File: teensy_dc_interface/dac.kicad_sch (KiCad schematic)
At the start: 10 parts, among them U1 AK4458VN

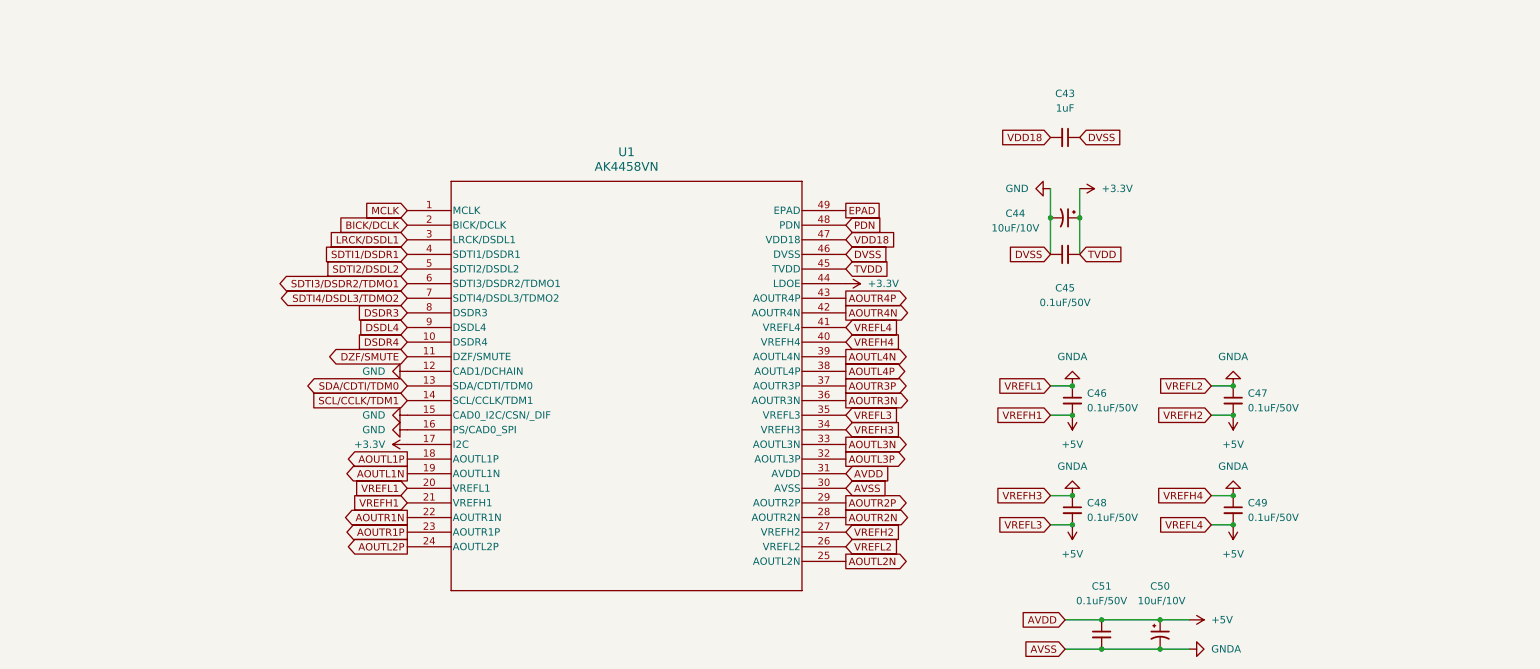
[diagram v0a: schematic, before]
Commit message: teensy to dac connections
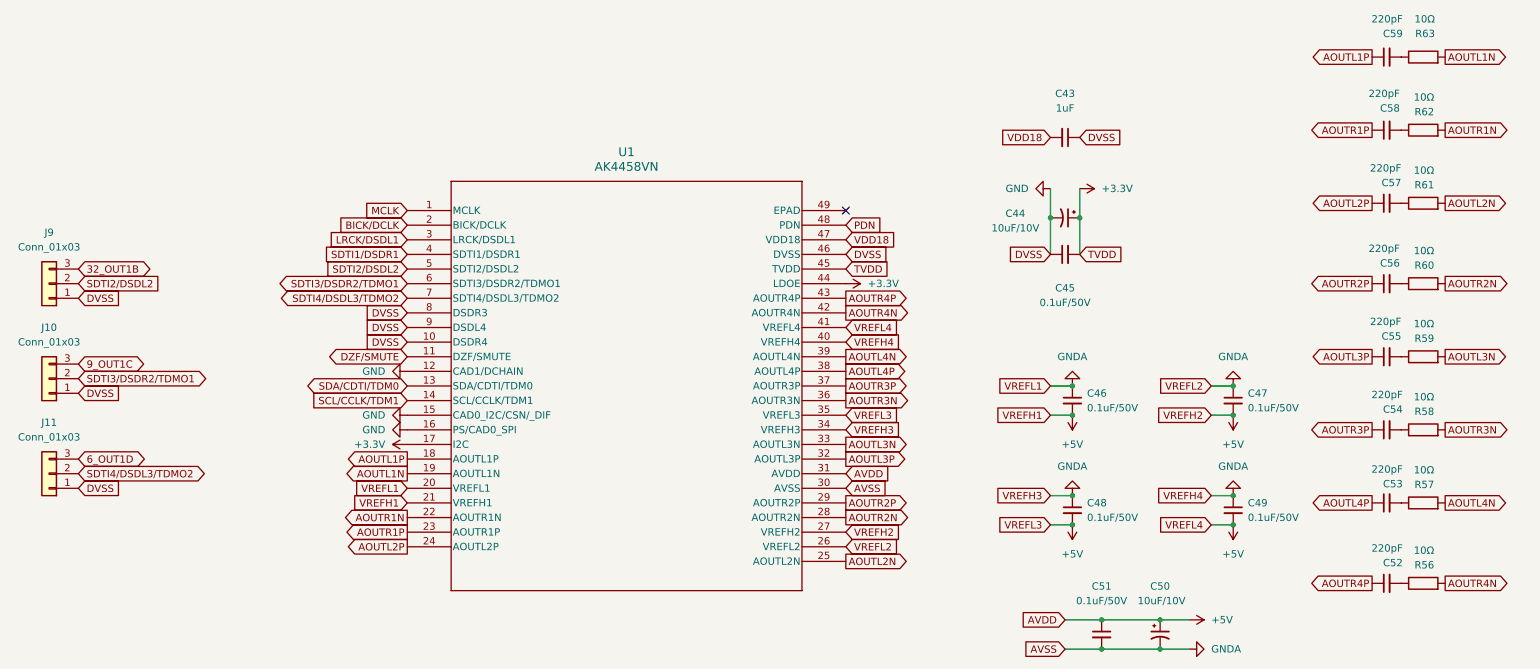
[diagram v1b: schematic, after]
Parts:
- added C52, C53, C54, C55, C56, C57, C58, C59: 220pF_0402_50V, 4ms_Capacitor:C_0402, symbol 4ms_Capacitor:220pF_0402_50V
- added J10, J11, J9: Conn_01x03, 4ms_Connector:Pins_1x03_2.54mm_TH, symbol 4ms_Connector:Conn_01x03
- added R56, R57, R58, R59, R60, R61, R62, R63: 10R_0402, 4ms_Resistor:R_0402, symbol 4ms_Resistor:10R_0402
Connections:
- net DSDL4 is gone; now on net GND: U1.9 (DSDL4)
- net DSDR3 is gone; now on net GND: U1.8 (DSDR3)
- net DSDR4 is gone; now on net GND: U1.10 (DSDR4)
- net AOUTL1N: now also R63.2
- net AOUTL1P: now also C59.1
- net AOUTL2N: now also R61.2
- net AOUTL2P: now also C57.1
- net AOUTL3N: now also R59.2
- net AOUTL3P: now also C55.1
- net AOUTL4N: now also R57.2
- net AOUTL4P: now also C53.1
- net AOUTR1N: now also R62.2
- net AOUTR1P: now also C58.1
- net AOUTR2N: now also R60.2
- net AOUTR2P: now also C56.1
- net AOUTR3N: now also R58.2
- net AOUTR3P: now also C54.1
- net AOUTR4N: now also R56.2
- net AOUTR4P: now also C52.1
- net GND: now also J10.1 (Pin_1), J11.1 (Pin_1), J9.1 (Pin_1)
- net SDTI2/DSDL2: now also J9.2 (Pin_2)
- net SDTI3/DSDR2/TDMO1: now also J10.2 (Pin_2)
- net SDTI4/DSDL3/TDMO2: now also J11.2 (Pin_2)
- net EPAD: no longer names the net of U1.49 (EPAD)
- new net: C55.2, R59.1
- new net: C54.2, R58.1
- new net: C57.2, R61.1
- new net: C59.2, R63.1
- new net: C52.2, R56.1
- new net: C58.2, R62.1
- new net: C53.2, R57.1
- new net: C56.2, R60.1
- new net 32_OUT1B: J9.3 (Pin_3)
- new net 6_OUT1D: J11.3 (Pin_3)
- new net 9_OUT1C: J10.3 (Pin_3)
- no-connect marks 0 -> 1

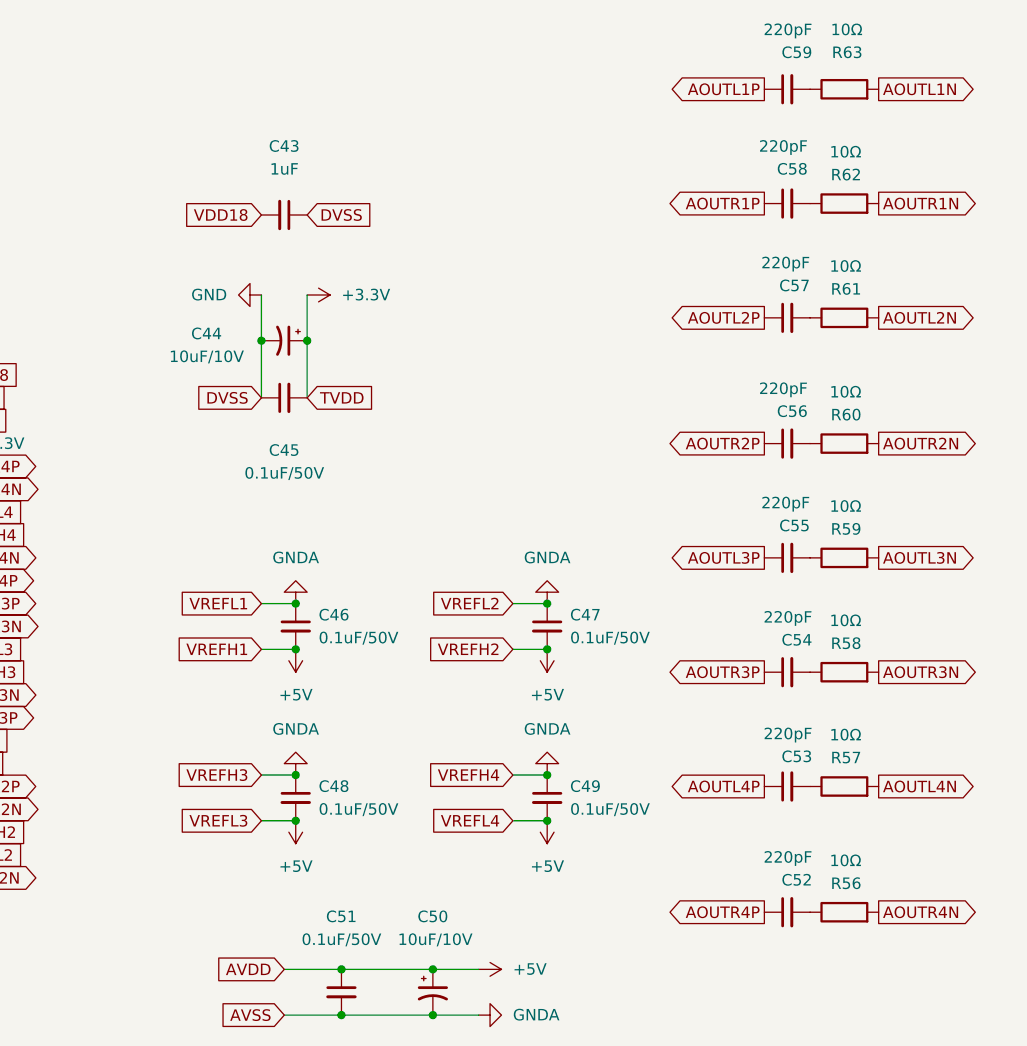
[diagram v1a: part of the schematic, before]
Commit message: Updated filtering between VREF's. Added separate power supply for Teensy on 5V. Added test points. Added ADC input
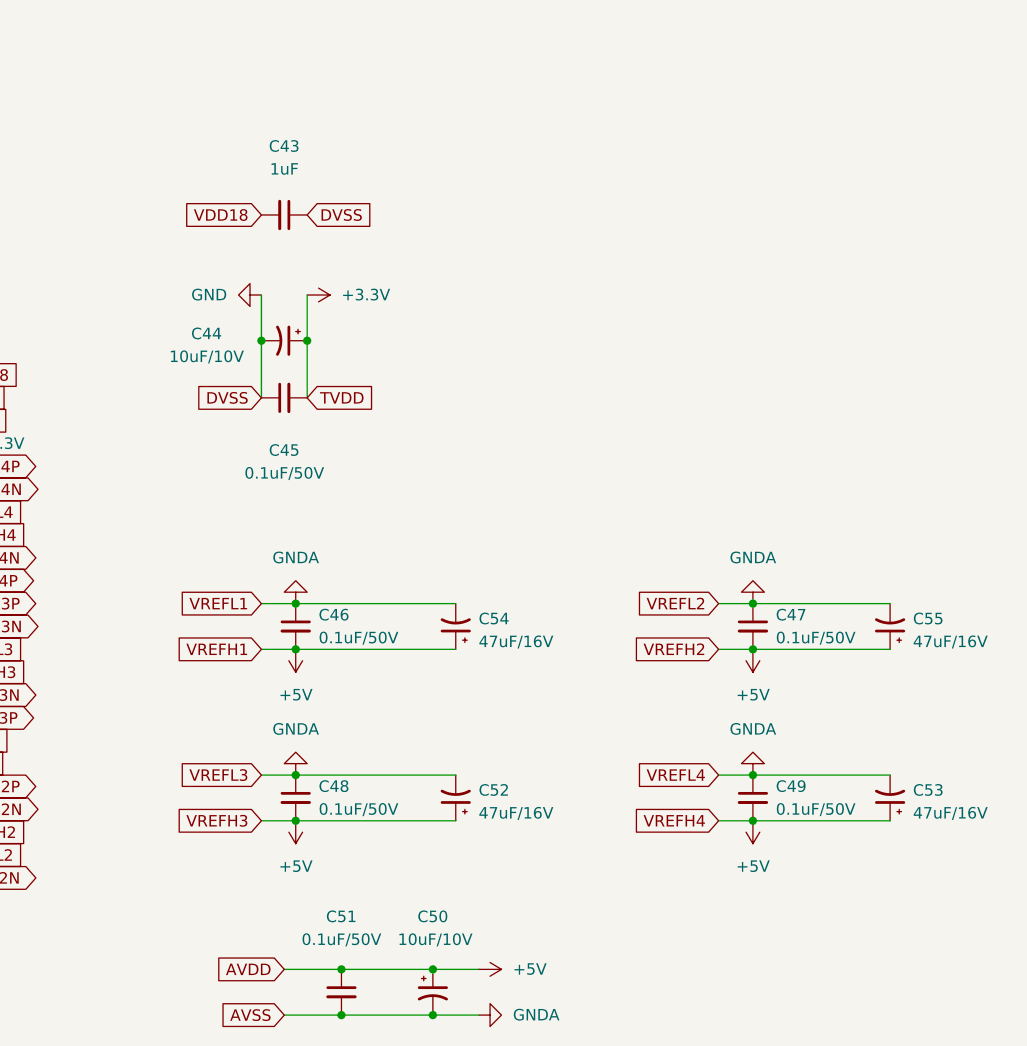
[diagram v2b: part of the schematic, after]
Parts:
- removed C52, C53, C54, C55, C56, C57, C58, C59: 220pF_0402_50V, 4ms_Capacitor:C_0402, symbol 4ms_Capacitor:220pF_0402_50V
- removed R56, R57, R58, R59, R60, R61, R62, R63: 10R_0402, 4ms_Resistor:R_0402, symbol 4ms_Resistor:10R_0402
- added C52, C53, C54, C55: 47uF_5x5.3_16V, 4ms_Capacitor:CP_Elec_5x5.3, symbol 4ms_Capacitor:47uF_5x5.3_16V
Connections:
- net +5V: now also U1.34 (VREFH3), U1.40 (VREFH4), C52.1, C53.1, C54.1, C55.1; no longer U1.35 (VREFL3), U1.41 (VREFL4)
- net GNDA: now also U1.35 (VREFL3), U1.41 (VREFL4), C52.2, C53.2, C54.2, C55.2; no longer U1.34 (VREFH3), U1.40 (VREFH4)
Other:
- moved on the sheet: C47, C49

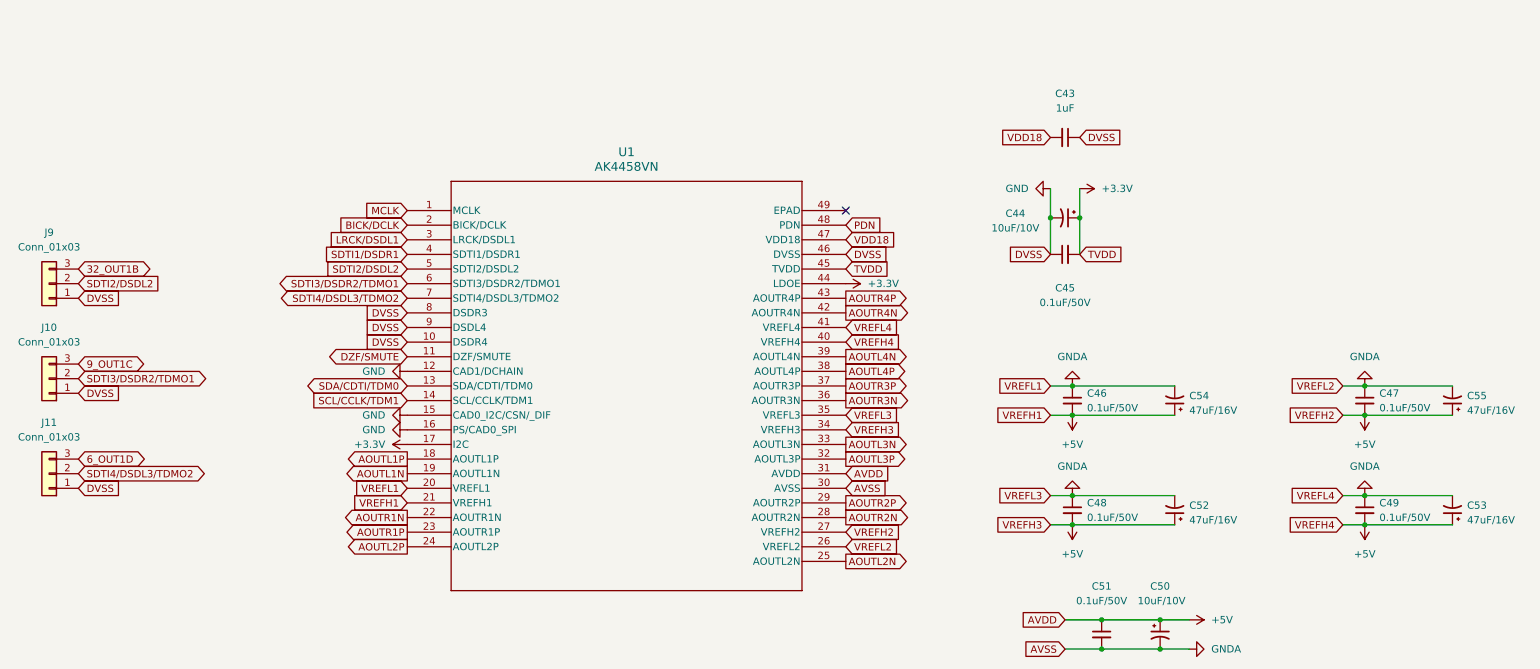
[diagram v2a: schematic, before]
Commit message: out pairs as pages
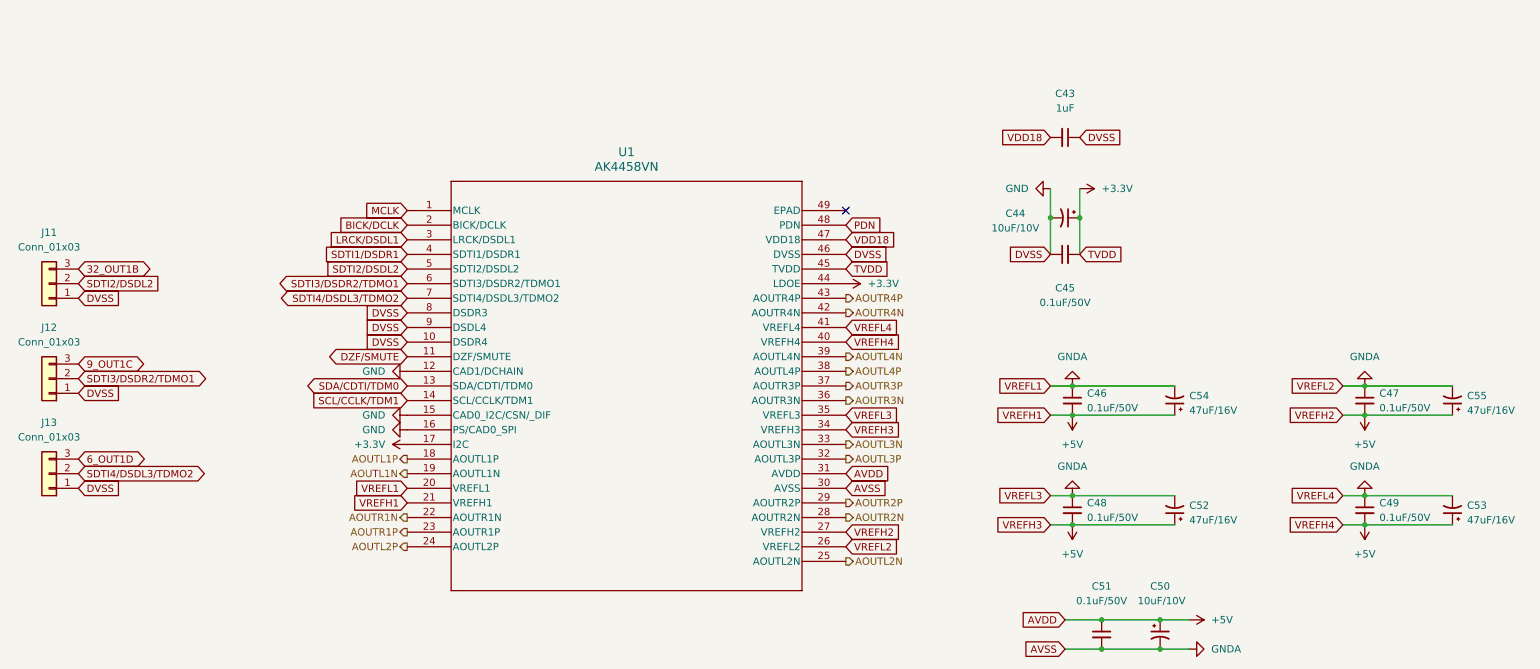
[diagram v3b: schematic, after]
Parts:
- renumbered J9 to J11, J10 to J12, J11 to J13

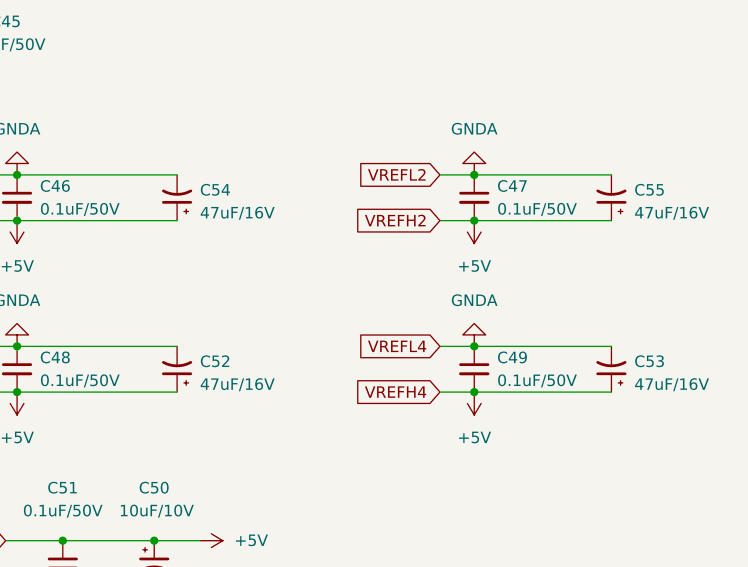
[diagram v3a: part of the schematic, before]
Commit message: Altered ground planes
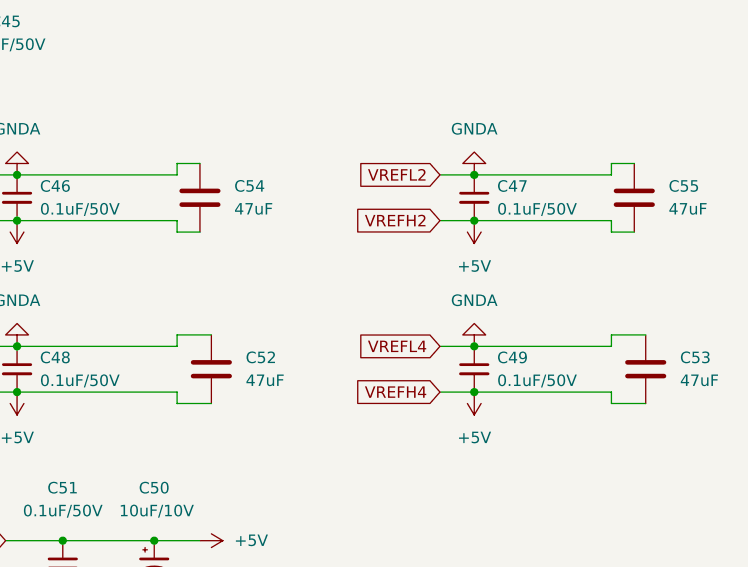
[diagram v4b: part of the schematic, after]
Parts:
- removed C52, C53, C54, C55: 47uF_5x5.3_16V, 4ms_Capacitor:CP_Elec_5x5.3, symbol 4ms_Capacitor:47uF_5x5.3_16V
- added C52, C53, C54, C55: 47uF, Capacitor_SMD:C_0805_2012Metric, symbol Device:C
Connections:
- net +5V: now also C52.2, C53.2, C54.2, C55.2
- net GNDA: now also C52.1, C53.1, C54.1, C55.1
